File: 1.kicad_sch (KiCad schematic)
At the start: 30 parts, among them J1 Screw_Terminal_01x03, J2 Screw_Terminal_01x01, J3 Screw_Terminal_01x01, J4 Conn_01x03_Pin, J5 Screw_Terminal_01x01, J6 Screw_Terminal_01x01, J7 Conn_01x01_Pin, J8 Conn_01x04_Pin, J9 Conn_01x01_Pin, U1 LTC2990

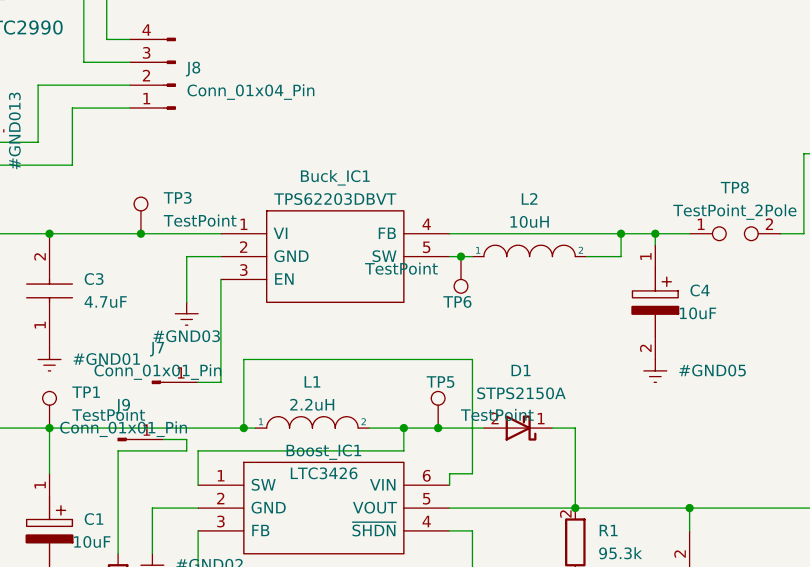
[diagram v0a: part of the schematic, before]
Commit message: Define edge cuts
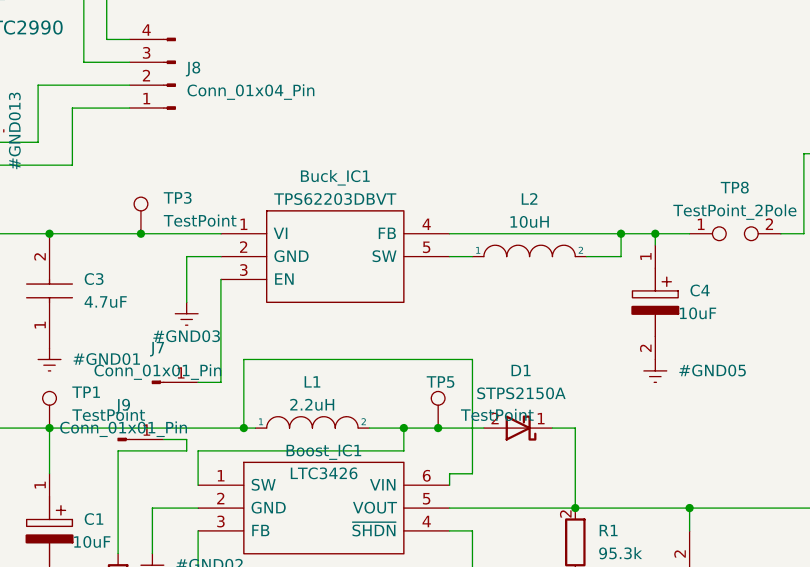
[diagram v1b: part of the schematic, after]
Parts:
- removed TP6: TestPoint, TestPoint:TestPoint_THTPad_1.5x1.5mm_Drill0.7mm, symbol Connector:TestPoint
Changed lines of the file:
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@@
   (junction (at 93.98 139.7) (diameter 0) (color 0 0 0 0)
   )
-  (junction (at 139.7 96.52) (diameter 0) (color 0 0 0 0)
-  )
   (junction (at 80.01 139.7) (diameter 0) (color 0 0 0 0)
   )
@@
     (stroke (width 0) (type default))
   )
-  (wire (pts (xy 138.43 96.52) (xy 139.7 96.52))
+  (wire (pts (xy 138.43 96.52) (xy 140.97 96.52))
     (stroke (width 0) (type default))
   )
@@
   )
   (wire (pts (xy 62.23 125.73) (xy 69.85 125.73))
-    (stroke (width 0) (type default))
-  )
-  (wire (pts (xy 139.7 96.52) (xy 140.97 96.52))
     (stroke (width 0) (type default))
   )
@@
         )
       )
-    )
-  )
-  (symbol (lib_id "Connector:TestPoint") (at 139.7 96.52 180) (unit 1)
-    (in_bom yes) (on_board yes) (dnp no)
-    (property "Reference" "TP6" (at 140.97 101.6 0)
-      (effects (font (size 1.27 1.27)) (justify left))
-    )
-    (property "Value" "TestPoint" (at 137.16 97.917 0)
-      (effects (font (size 1.27 1.27)) (justify left))
-    )
-    (property "Footprint" "TestPoint:TestPoint_THTPad_1.5x1.5mm_Drill0.7mm" (at 134.62 96.52 0)
-      (effects (font (size 1.27 1.27)) hide)
-    )
-    (property "Datasheet" "~" (at 134.62 96.52 0)
-      (effects (font (size 1.27 1.27)) hide)
-    )
-    (pin "1")
-    (instances
-      (project "1"
-        (path "/c93af209-ee06-4b35-8e6a-15ea4826ac18"
-          (reference "TP6") (unit 1)
-        )
-      )

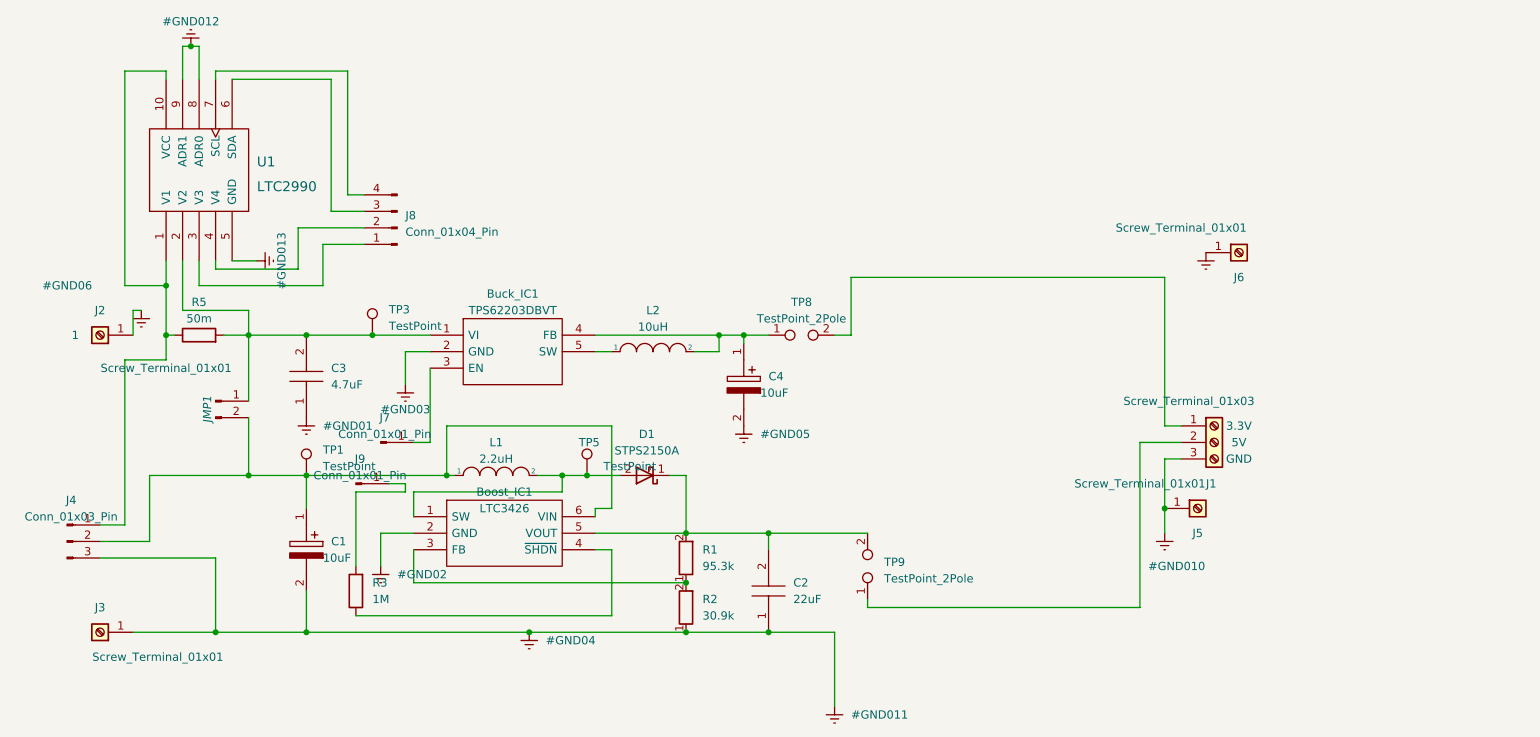
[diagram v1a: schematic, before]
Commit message: Add protection circ
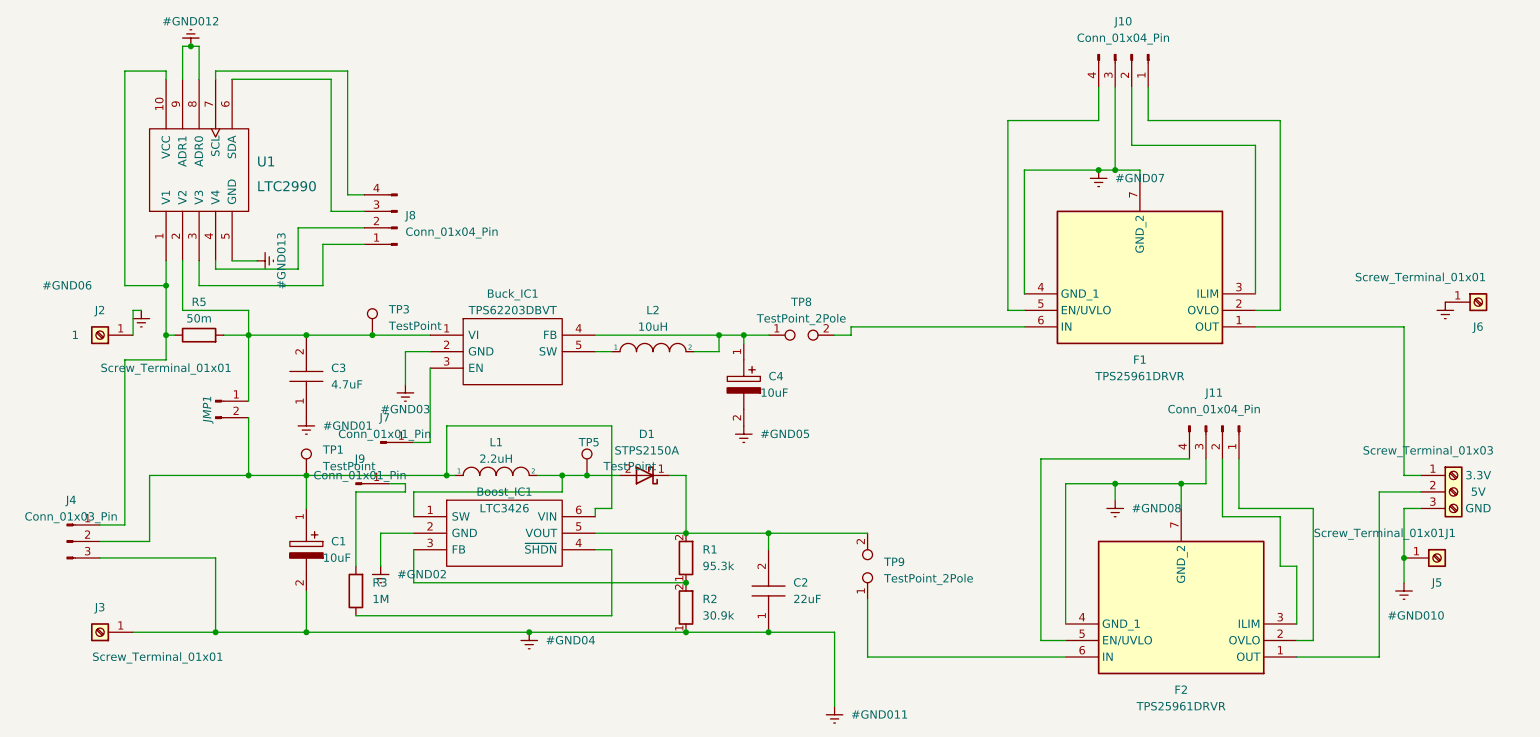
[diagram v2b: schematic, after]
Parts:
- added F1, F2: TPS25961DRVR, PROTECC:SON65P200X200X80-7N, symbol TPS25961DRVR:TPS25961DRVR
- added J10, J11: Conn_01x04_Pin, Connector_PinHeader_2.54mm:PinHeader_1x04_P2.54mm_Vertical, symbol Connector:Conn_01x04_Pin
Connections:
- net Earth: now also F1.4 (GND_1), F1.7 (GND_2), F2.4 (GND_1), F2.7 (GND_2), J10.3 (Pin_3), J11.3 (Pin_3)
- net at J1.1 (Pin_1): now also F1.1 (OUT); no longer TP8.2
- net at J1.2 (Pin_2): now also F2.1 (OUT); no longer TP9.1
- new net: F1.6 (IN), TP8.2
- new net: F2.2 (OVLO), J11.1 (Pin_1)
- new net: F2.3 (ILIM), J11.2 (Pin_2)
- new net: F2.5 (EN/UVLO), J11.4 (Pin_4)
- new net: F2.6 (IN), TP9.1
- new net: F1.2 (OVLO), J10.1 (Pin_1)
- new net: F1.3 (ILIM), J10.2 (Pin_2)
- new net: F1.5 (EN/UVLO), J10.4 (Pin_4)
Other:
- moved on the sheet: J1, J5, J6
